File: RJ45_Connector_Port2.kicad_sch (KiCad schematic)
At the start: 8 parts, among them J1 0826-1X4T-43-F

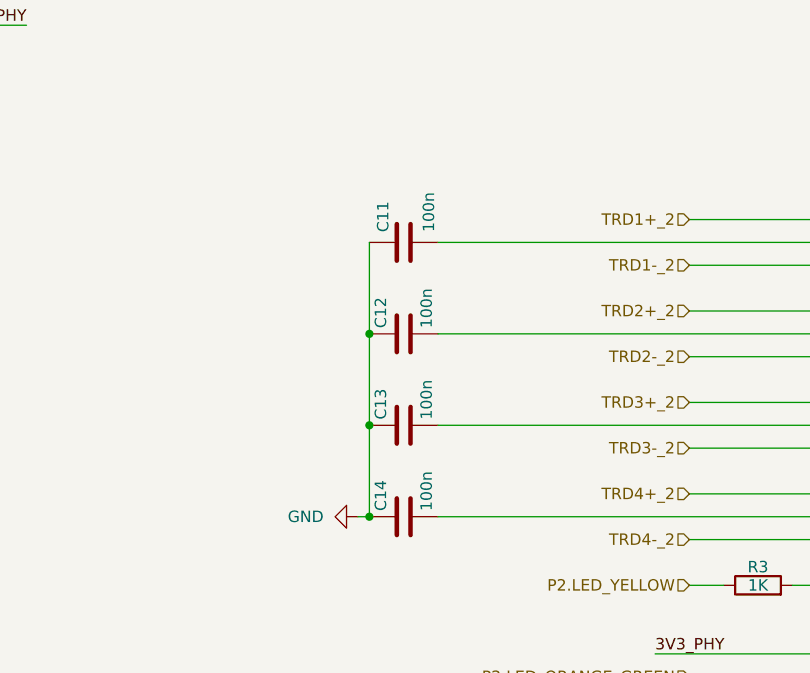
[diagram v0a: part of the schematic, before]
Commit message: updates symbols and fixes ERC errors. Refs: #9
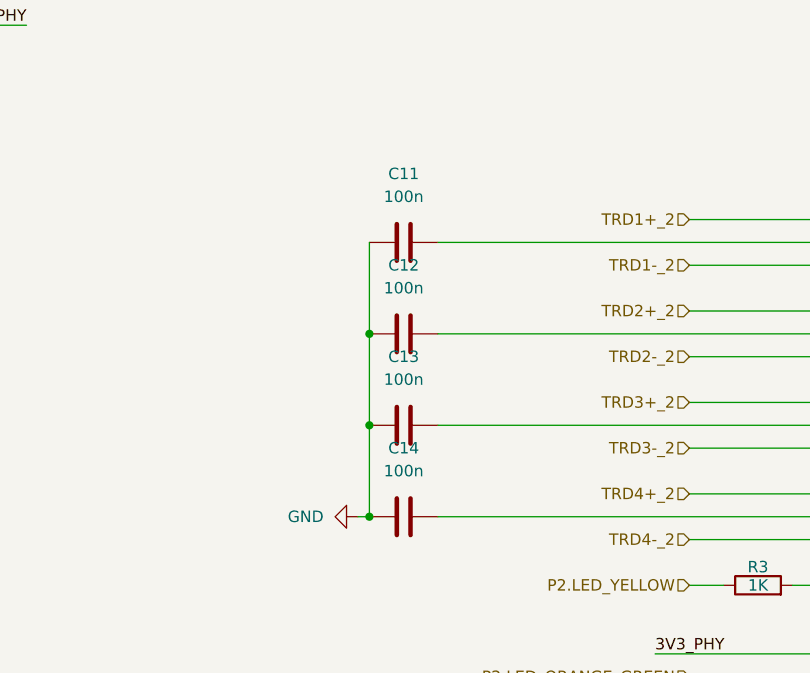
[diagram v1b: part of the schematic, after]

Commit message: updates RJ45_Connector_Port2. Refs: #41
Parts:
- C11, C12, C13, C14: symbol KL_C:C_100n_50V_X7R_0603_10 -> KL_C:C_100n_50V_10pct_X7R_0603; Dielectric (none) -> X7R; MPN (none) -> CL10B104KB8NNNC; Package_in_inch (none) -> 0603; Tolerance 20 -> (none); Tolerance_in_pct (none) -> 10; Voltage 10 -> (none); Voltage_in_V (none) -> 50
- J1: value 0826-1X4T-43-F -> RJ45_0826-1X4T-43-F; symbol KL_Connectors_RJ45:0826-1X4T-43-F -> KL_Conn_Data:RJ45_0826-1X4T-43-F; MANUFACTURER Bel Fuse -> (none); MAXIMUM_PACKAGE_HEIGHT 15.49mm -> (none); MPN (none) -> 0826-1X4T-43-F; PARTREV D -> (none); STANDARD Manufacturer Recommendations -> (none)
- R3, R4, R8: symbol KL_R:R_1K_100mW_5_0603 -> KL_R:R_1K_0.1W_5pct_0603; MPN (none) -> CRGCQ0603J1K0; Package (in) 0603 -> (none); Package_in_inch (none) -> 0603; Power 100mW -> (none); Power_in_W (none) -> 0.1; Tolerance 5 -> (none); Tolerance_in_pct (none) -> 5
